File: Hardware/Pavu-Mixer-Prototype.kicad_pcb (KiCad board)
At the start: 2 copper layers, 155.9 x 91.9 mm, 66 parts, among them J1 Conn_02x16_Odd_Even, U1 74HC595, U2 74HC595, U3 74HC595, U4 PCA9555D, U5 PCA9536D

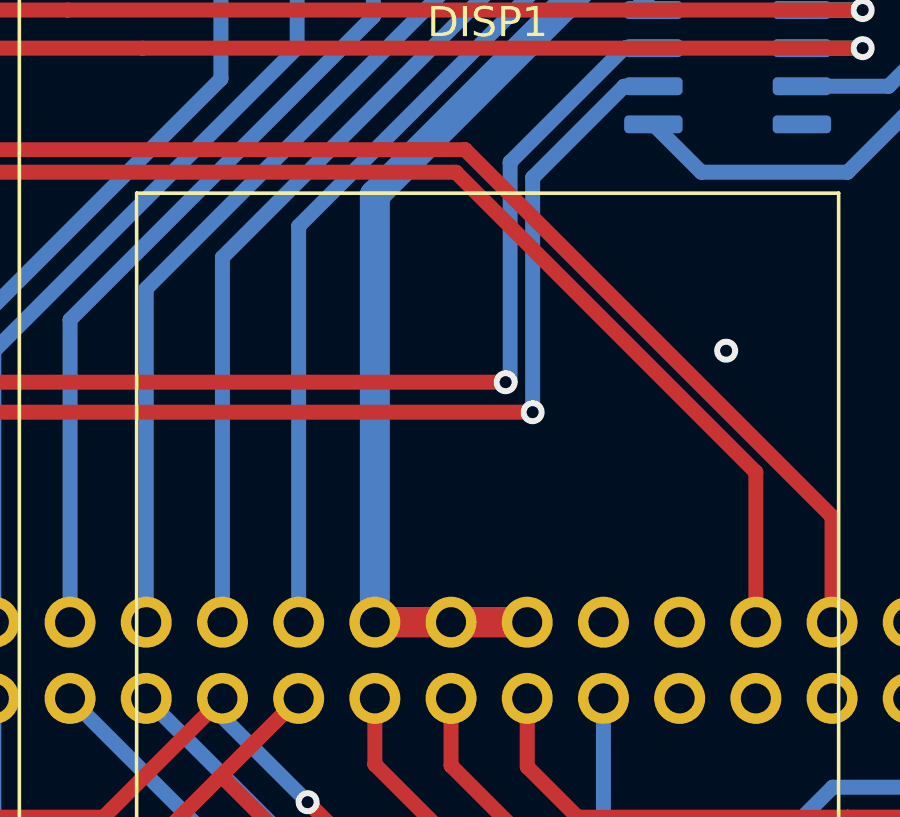
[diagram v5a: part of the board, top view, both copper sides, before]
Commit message: Add I2C Pull-Up Resistors
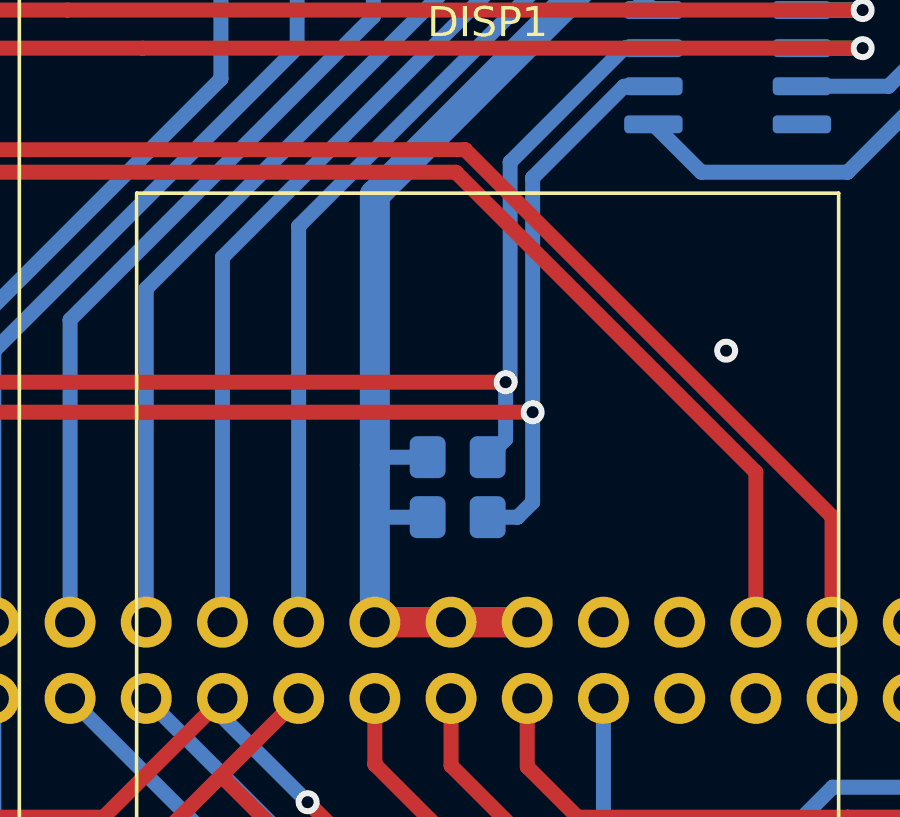
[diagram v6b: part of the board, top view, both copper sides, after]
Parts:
- added R36: 1k, Resistor_SMD:R_0805_2012Metric_Pad1.20x1.40mm_HandSolder, B.Cu at (129.0, 86.5)
- added R37: 1k, Resistor_SMD:R_0805_2012Metric_Pad1.20x1.40mm_HandSolder, B.Cu at (129.0, 84.5)
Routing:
- net I2C_SCL: track 110.5 -> 115.2 mm
- net +3V3: track 467.8 -> 471.4 mm
- net I2C_SDA: track 114.9 -> 117.6 mm
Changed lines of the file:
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@@
     (thickness 1.6)
     (drawings 7)
-    (tracks 661)
+    (tracks 670)
     (zones 0)
-    (modules 66)
+    (modules 68)
     (nets 100)
   )
@@
   )
   (setup
-    (last_trace_width 0.25)
+    (last_trace_width 0.5)
     (user_trace_width 0.1)
     (user_trace_width 0.2)
@@
   )
   (module Resistor_SMD:R_0805_2012Metric_Pad1.20x1.40mm_HandSolder (layer B.Cu)
+    (at 129 84.5 180)
+    (descr "Resistor SMD 0805 (2012 Metric), square (rectangular) end terminal, IPC_7351 nominal with elongated pad for handsoldering. (Body size source: IPC-SM-782 page 72, https://www.pcb-3d.com/wordpress/wp-content/uploads/ipc-sm-782a_amendment_1_and_2.pdf), generated with kicad-footprint-generator")
+    (tags "resistor handsolder")
+    (attr smd)
+    (fp_text reference R37 (at -4.5 0) (layer B.SilkS)
+      (effects (font (size 1 1) (thickness 0.15)) (justify mirror))
+    )
+    (fp_text value 1k (at 0 -1.65) (layer B.Fab)
+      (effects (font (size 1 1) (thickness 0.15)) (justify mirror))
+    )
+    (fp_text user %R (at 0 0) (layer B.Fab)
+      (effects (font (size 0.5 0.5) (thickness 0.08)) (justify mirror))
+    )
+    (fp_line (start -1 -0.625) (end -1 0.625) (layer B.Fab) (width 0.1))
+    (fp_line (start -1 0.625) (end 1 0.625) (layer B.Fab) (width 0.1))
+    (fp_line (start 1 0.625) (end 1 -0.625) (layer B.Fab) (width 0.1))
+    (fp_line (start 1 -0.625) (end -1 -0.625) (layer B.Fab) (width 0.1))
+    (fp_line (start -0.227064 0.735) (end 0.227064 0.735) (layer B.SilkS) (width 0.12))
+    (fp_line (start -0.227064 -0.735) (end 0.227064 -0.735) (layer B.SilkS) (width 0.12))
+    (fp_line (start -1.85 -0.95) (end -1.85 0.95) (layer B.CrtYd) (width 0.05))
+    (fp_line (start -1.85 0.95) (end 1.85 0.95) (layer B.CrtYd) (width 0.05))
+    (fp_line (start 1.85 0.95) (end 1.85 -0.95) (layer B.CrtYd) (width 0.05))
+    (fp_line (start 1.85 -0.95) (end -1.85 -0.95) (layer B.CrtYd) (width 0.05))
+    (pad 2 smd roundrect (at 1 0 180) (size 1.2 1.4) (layers B.Cu B.Paste B.Mask) (roundrect_rratio 0.208333)
+      (net 52 +3V3))
+    (pad 1 smd roundrect (at -1 0 180) (size 1.2 1.4) (layers B.Cu B.Paste B.Mask) (roundrect_rratio 0.208333)
+      (net 68 I2C_SDA))
+    (model ${KISYS3DMOD}/Resistor_SMD.3dshapes/R_0805_2012Metric.wrl
+      (at (xyz 0 0 0))
+      (scale (xyz 1 1 1))
+      (rotate (xyz 0 0 0))
+    )
+  )
+  (module Resistor_SMD:R_0805_2012Metric_Pad1.20x1.40mm_HandSolder (layer B.Cu)
+    (at 129 86.5 180)
+    (descr "Resistor SMD 0805 (2012 Metric), square (rectangular) end terminal, IPC_7351 nominal with elongated pad for handsoldering. (Body size source: IPC-SM-782 page 72, https://www.pcb-3d.com/wordpress/wp-content/uploads/ipc-sm-782a_amendment_1_and_2.pdf), generated with kicad-footprint-generator")
+    (tags "resistor handsolder")
+    (attr smd)
+    (fp_text reference R36 (at -4.5 0) (layer B.SilkS)
+      (effects (font (size 1 1) (thickness 0.15)) (justify mirror))
+    )
+    (fp_text value 1k (at 0 -1.65) (layer B.Fab)
+      (effects (font (size 1 1) (thickness 0.15)) (justify mirror))
+    )
+    (fp_text user %R (at 0 0) (layer B.Fab)
+      (effects (font (size 0.5 0.5) (thickness 0.08)) (justify mirror))
+    )
+    (fp_line (start -1 -0.625) (end -1 0.625) (layer B.Fab) (width 0.1))
+    (fp_line (start -1 0.625) (end 1 0.625) (layer B.Fab) (width 0.1))
+    (fp_line (start 1 0.625) (end 1 -0.625) (layer B.Fab) (width 0.1))
+    (fp_line (start 1 -0.625) (end -1 -0.625) (layer B.Fab) (width 0.1))
+    (fp_line (start -0.227064 0.735) (end 0.227064 0.735) (layer B.SilkS) (width 0.12))
+    (fp_line (start -0.227064 -0.735) (end 0.227064 -0.735) (layer B.SilkS) (width 0.12))
+    (fp_line (start -1.85 -0.95) (end -1.85 0.95) (layer B.CrtYd) (width 0.05))
+    (fp_line (start -1.85 0.95) (end 1.85 0.95) (layer B.CrtYd) (width 0.05))
+    (fp_line (start 1.85 0.95) (end 1.85 -0.95) (layer B.CrtYd) (width 0.05))
+    (fp_line (start 1.85 -0.95) (end -1.85 -0.95) (layer B.CrtYd) (width 0.05))
+    (pad 2 smd roundrect (at 1 0 180) (size 1.2 1.4) (layers B.Cu B.Paste B.Mask) (roundrect_rratio 0.208333)
+      (net 52 +3V3))
+    (pad 1 smd roundrect (at -1 0 180) (size 1.2 1.4) (layers B.Cu B.Paste B.Mask) (roundrect_rratio 0.208333)
+      (net 67 I2C_SCL))
+    (model ${KISYS3DMOD}/Resistor_SMD.3dshapes/R_0805_2012Metric.wrl
+      (at (xyz 0 0 0))
+      (scale (xyz 1 1 1))
+      (rotate (xyz 0 0 0))
+    )
+  )
+  (module Resistor_SMD:R_0805_2012Metric_Pad1.20x1.40mm_HandSolder (layer B.Cu)
     (at 130 138 180)
     (descr "Resistor SMD 0805 (2012 Metric), square (rectangular) end terminal, IPC_7351 nominal with elongated pad for handsoldering. (Body size source: IPC-SM-782 page 72, https://www.pcb-3d.com/wordpress/wp-content/uploads/ipc-sm-782a_amendment_1_and_2.pdf), generated with kicad-footprint-generator")
@@
   (segment (start 110 66.5) (end 144.5 66.5) (width 1) (layer F.Cu) (net 52))
   (segment (start 144.5 66.5) (end 152.5 66.5) (width 1) (layer F.Cu) (net 52))
-  (segment (start 126.24 90) (end 126.24 75.76) (width 1) (layer B.Cu) (net 52))
   (segment (start 134 68.07) (end 134 68) (width 0.5) (layer B.Cu) (net 52))
   (segment (start 135.525 69.595) (end 134 68.07) (width 0.5) (layer B.Cu) (net 52))
@@
   (segment (start 134.65 136.35) (end 133 138) (width 0.5) (layer B.Cu) (net 52))
   (segment (start 133 138) (end 131 138) (width 0.5) (layer B.Cu) (net 52))
+  (segment (start 126.5 84.5) (end 126.24 84.76) (width 0.5) (layer B.Cu) (net 52))
+  (segment (start 128 84.5) (end 126.5 84.5) (width 0.5) (layer B.Cu) (net 52))
+  (segment (start 126.24 84.76) (end 126.24 75.76) (width 1) (layer B.Cu) (net 52))
+  (segment (start 126.24 90) (end 126.24 84.76) (width 1) (layer B.Cu) (net 52))
+  (segment (start 128 86.5) (end 126.24 86.5) (width 0.5) (layer B.Cu) (net 52))
   (segment (start 126.19 69.81) (end 126.19 62.5) (width 0.5) (layer B.Cu) (net 53))
   (segment (start 116.08 79.92) (end 126.19 69.81) (width 0.5) (layer B.Cu) (net 53))
@@
   (via (at 124 96) (size 0.8) (drill 0.4) (layers F.Cu B.Cu) (net 67))
   (segment (start 124 96) (end 121 93) (width 0.5) (layer B.Cu) (net 67))
+  (segment (start 131.5 83) (end 131.5 86) (width 0.5) (layer B.Cu) (net 67))
+  (segment (start 131.5 86) (end 131 86.5) (width 0.5) (layer B.Cu) (net 67))
+  (segment (start 131 86.5) (end 130 86.5) (width 0.5) (layer B.Cu) (net 67))
   (segment (start 134.55 70.865) (end 130.74999 74.66501) (width 0.5) (layer B.Cu) (net 68))
   (segment (start 135.525 70.865) (end 134.55 70.865) (width 0.5) (layer B.Cu) (net 68))
@@
   (segment (start 121.12 95.12) (end 118.98999 97.25001) (width 0.5) (layer F.Cu) (net 68))
   (segment (start 123.7 92.54) (end 121.12 95.12) (width 0.5) (layer F.Cu) (net 68))
+  (segment (start 130.6 82) (end 130.6 83.9) (width 0.5) (layer B.Cu) (net 68))
+  (segment (start 130.6 83.9) (end 130 84.5) (width 0.5) (layer B.Cu) (net 68))
   (segment (start 213.475 112.365) (end 216.5 112.365) (width 0.5) (layer B.Cu) (net 69))
   (via (at 216.5 112.365) (size 0.8) (drill 0.4) (layers F.Cu B.Cu) (net 69))

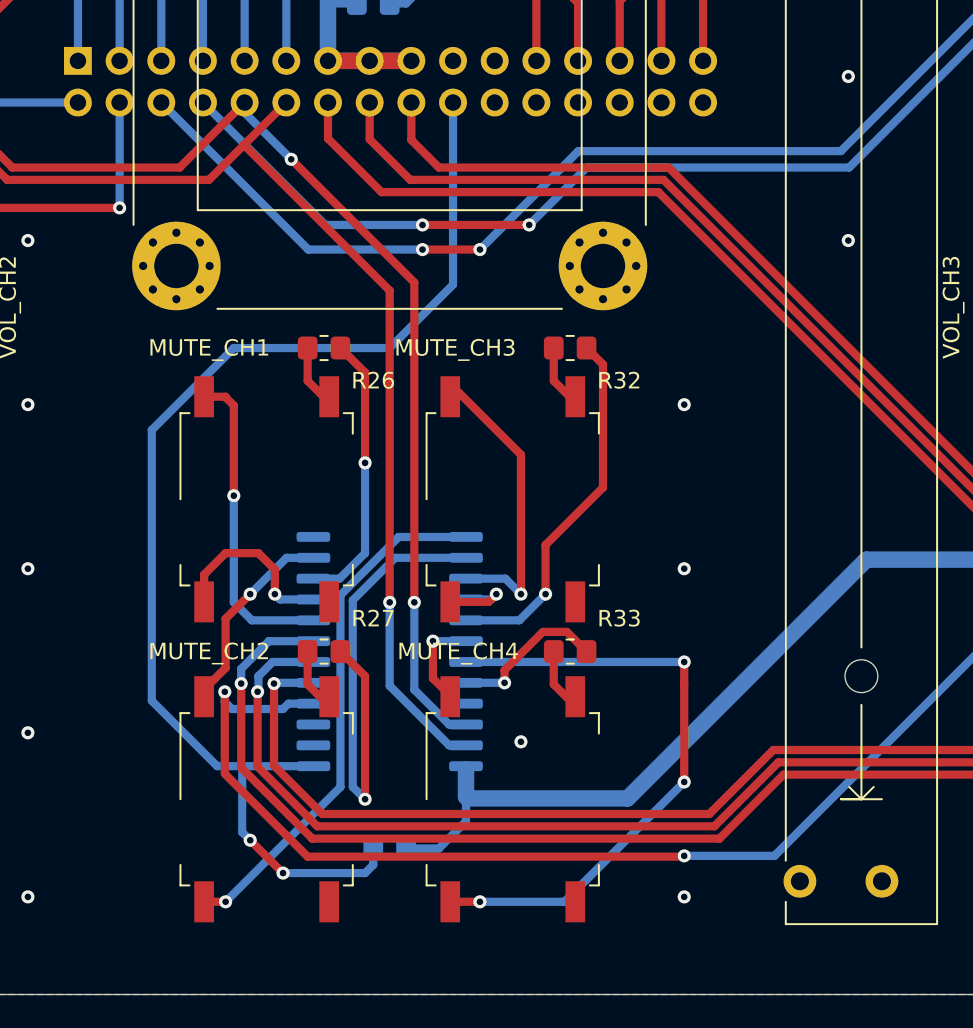
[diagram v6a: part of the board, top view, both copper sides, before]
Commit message: Add mute button pull-ups
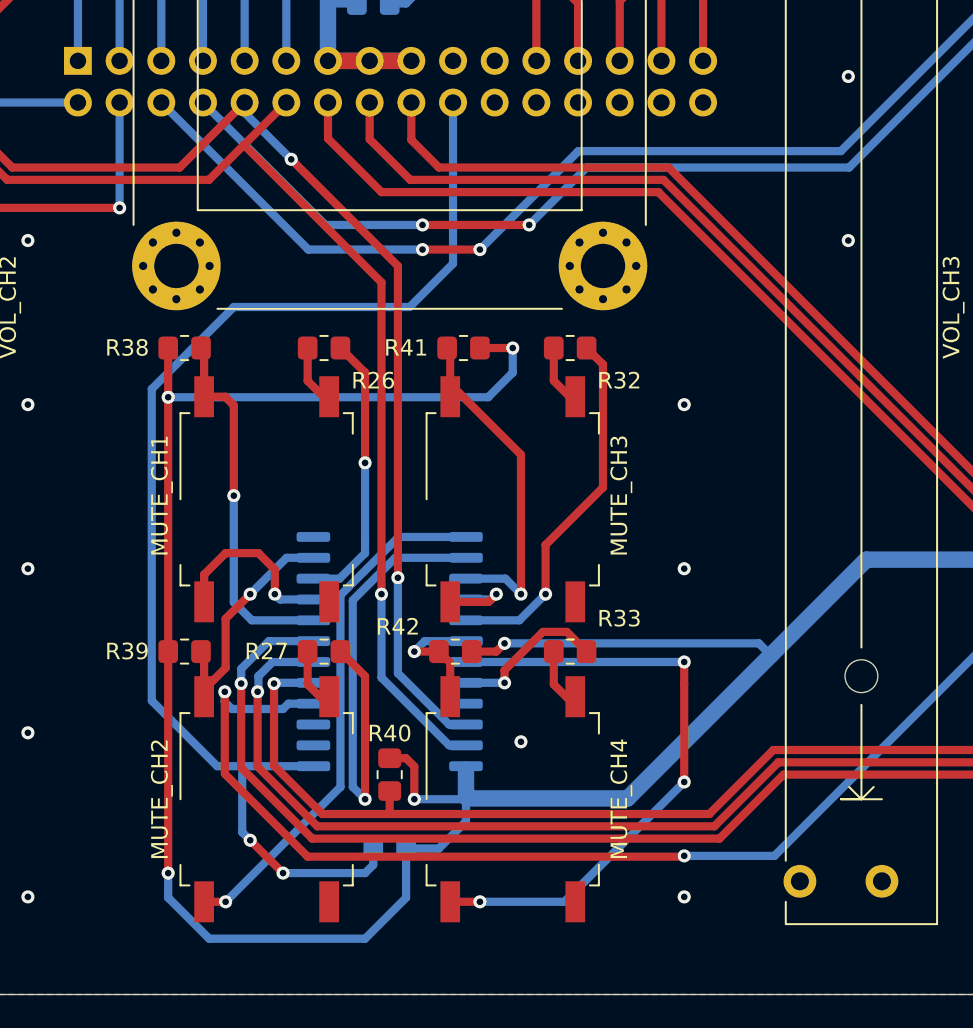
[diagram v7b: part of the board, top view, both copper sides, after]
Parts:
- added R38: 1k, Resistor_SMD:R_0805_2012Metric_Pad1.20x1.40mm_HandSolder, F.Cu at (117.5, 107.5)
- added R39: 1k, Resistor_SMD:R_0805_2012Metric_Pad1.20x1.40mm_HandSolder, F.Cu at (117.5, 126.0)
- added R40: 1k, Resistor_SMD:R_0805_2012Metric_Pad1.20x1.40mm_HandSolder, F.Cu at (130.0, 133.5)
- added R41: 1k, Resistor_SMD:R_0805_2012Metric_Pad1.20x1.40mm_HandSolder, F.Cu at (134.5, 107.5)
- added R42: 1k, Resistor_SMD:R_0805_2012Metric_Pad1.20x1.40mm_HandSolder, F.Cu at (134.0, 126.0)
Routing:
- net +3V3: track 471.4 -> 575.2 mm, vias 1 -> 6
- net /MUTE3_BTN: track 17.9 -> 20.7 mm
- net /MUTE1_BTN: track 19.4 -> 22.1 mm
- net /MUTE2_BTN: track 11.3 -> 13.9 mm
- net /MUTE4_BTN: track 5.51 -> 7.95 mm
- net /MUTE_MAIN_BTN: track 77.3 -> 78.7 mm
- net PCA_INT: track 75.4 -> 76.1 mm

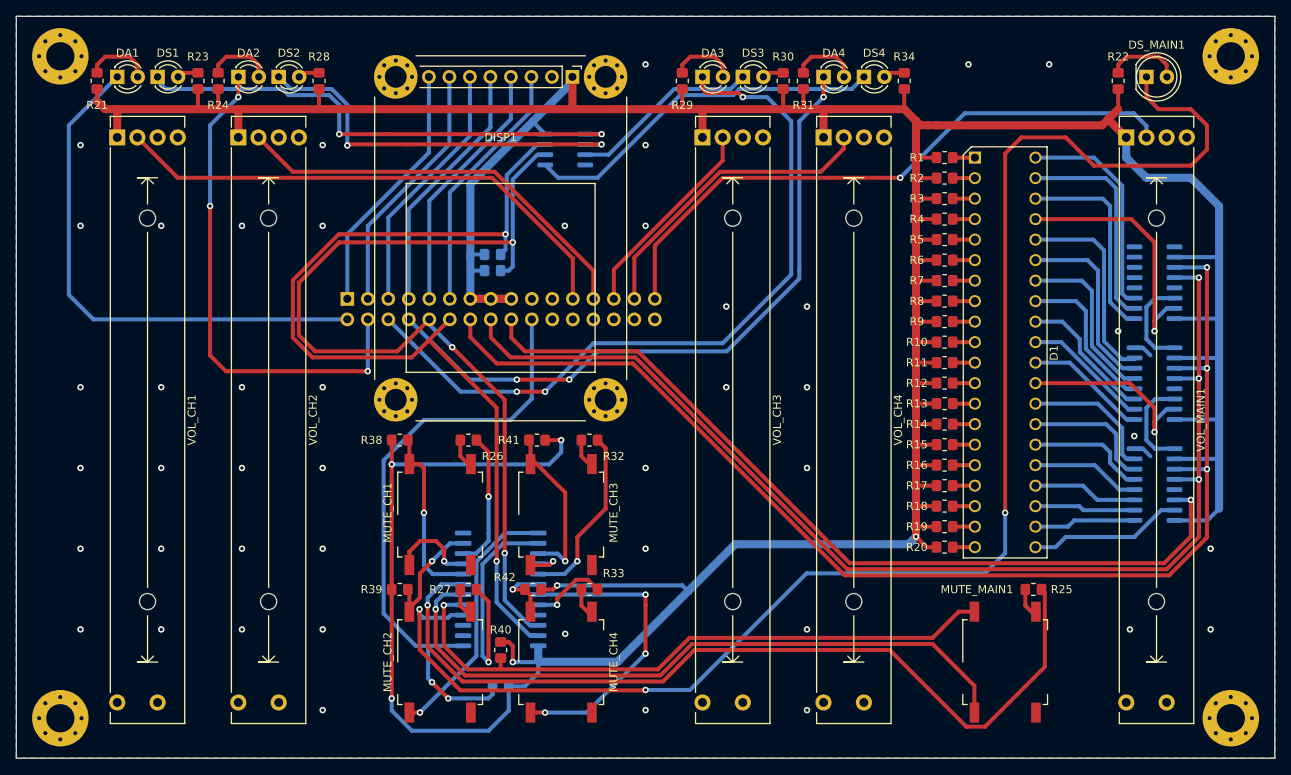
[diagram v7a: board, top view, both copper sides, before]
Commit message: Move resistors to the backside and reroute everything
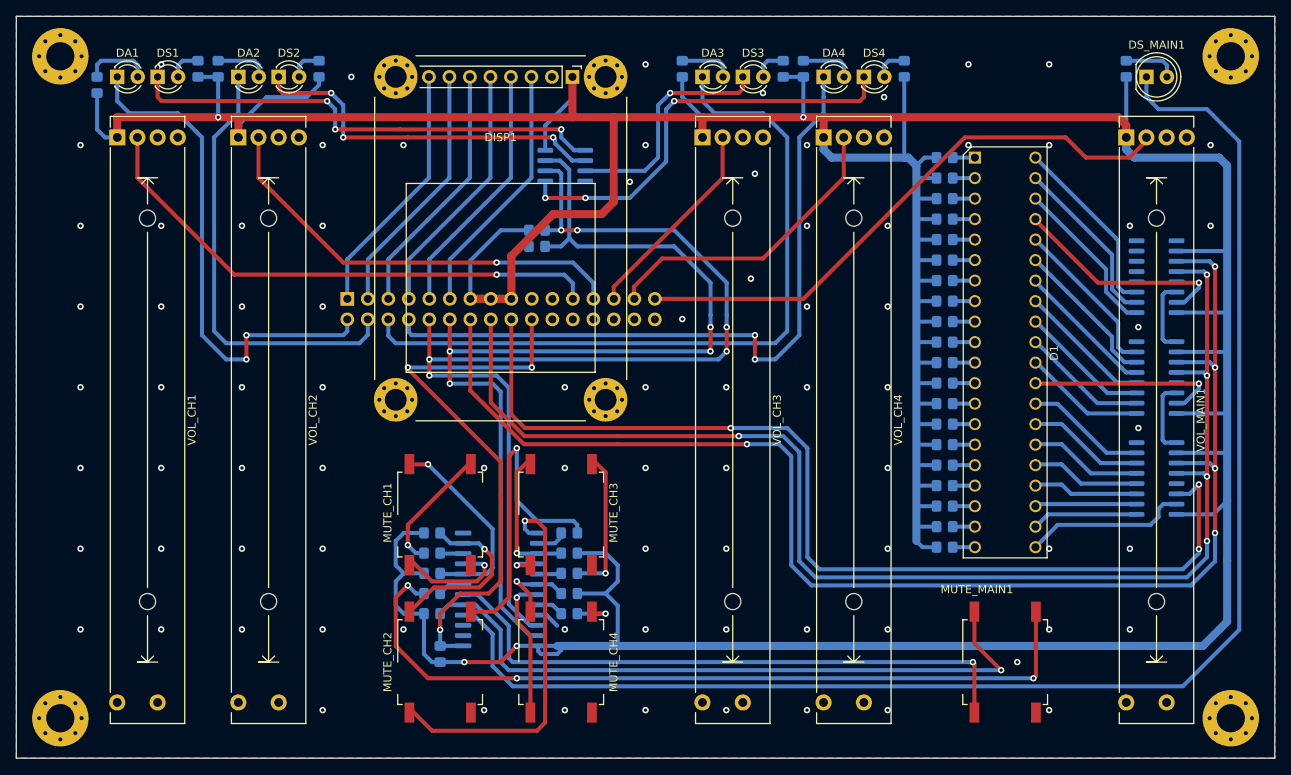
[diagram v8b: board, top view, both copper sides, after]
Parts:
- R1, R10, R11, R12, R13, R14, R15, R16, R17, R18, R19, R2, R20, R21, R22, R23, R24, R25, R26, R27, R28, R29, R3, R30, R31, R32, R33, R34, R38, R39, R4, R40, R41, R42, R5, R6, R7, R8, R9: moved to B.Cu
- moved R25 74.5 mm to (121.5, 126.5)
- moved R38 17.0 mm to (121.5, 124.0)
- moved R32 16.7 mm to (138.5, 124.0), turned to 180 degrees
- moved R26 14.7 mm to (121.5, 121.5)
- moved R41 14.6 mm to (138.5, 121.5)
- moved R27 14.3 mm to (138.5, 119.0), turned to 180 degrees
- moved R40 9.62 mm to (121.5, 129.0), turned to 0 degrees
- moved R35 8.50 mm to (122.5, 134.0), turned to 90 degrees
- moved R39 8.06 mm to (121.5, 119.0)
- moved R36 7.43 mm to (134.5, 81.5)
- moved R37 5.59 mm to (134.5, 83.5)
- moved R42 4.53 mm to (138.5, 126.5)
- moved R33 3.91 mm to (138.5, 129.0), turned to 180 degrees
- moved U5 2.00 mm to (138.0, 73.5)
- moved R22 1.80 mm to (207.5, 61.5)
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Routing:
- net /MUTE_MAIN_LED2: track 107.8 -> 3.32 mm, vias 1 -> 0
- net Net-(MUTE_MAIN1-Pad3): track 3.41 -> 99.6 mm, vias 0 -> 3
- net +3V3: track 575.2 -> 644.0 mm, vias 6 -> 4
- net Net-(MUTE_CH2-Pad3): track 3.41 -> 40.6 mm, vias 0 -> 1
- net /MUTE2_LED2: track 30.0 -> 3.68 mm, vias 1 -> 0
- net /MUTE4_LED1: track 37.9 -> 17.8 mm, vias 3 -> 1
- net /MUTE3_LED2: track 22.4 -> 2.75 mm, vias 1 -> 0
- net MAINVOL_SER: track 106.0 -> 125.4 mm, vias 1 -> 3
- net MAINVOL_RCLK: track 144.9 -> 163.9 mm, vias 3 -> 5
- net MAINVOL_SRCLK: track 153.3 -> 171.9 mm, vias 3 -> 5
- net /MUTE2_LED1: track 32.0 -> 47.7 mm
- net Net-(MUTE_CH3-Pad3): track 3.41 -> 18.1 mm, vias 0 -> 1
- net /MUTE1_LED2: track 16.9 -> 2.79 mm, vias 1 -> 0
- net I2C_SCL: track 115.2 -> 129.1 mm, vias 3 -> 6
- net Net-(MUTE_CH1-Pad3): track 3.41 -> 15.5 mm, vias 0 -> 1
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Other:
- board text added: "Pavu-Mixer Rev 1.0 2021-03-30 Rahix"
- board text removed: "Pavu-Mixer Rev 1.0 2021-03-29 Rahix"
